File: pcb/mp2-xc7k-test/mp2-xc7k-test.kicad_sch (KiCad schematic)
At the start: 5 parts, among them M5 MECHANICAL, M6 MECHANICAL, M7 MECHANICAL, M8 MECHANICAL, M9 MECHANICAL

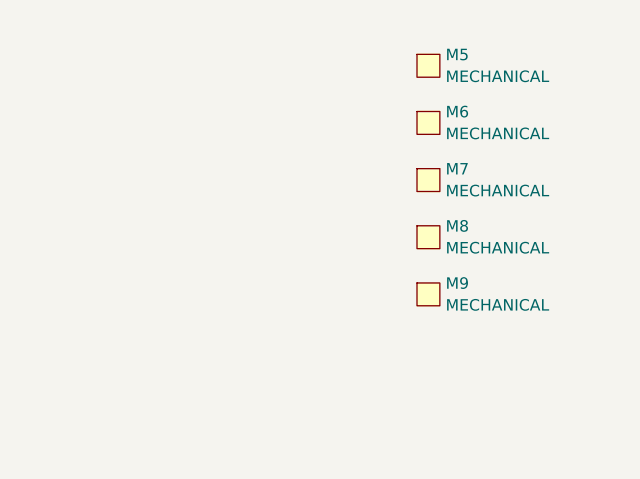
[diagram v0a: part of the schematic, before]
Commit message: Continued layout, 454 unrouted
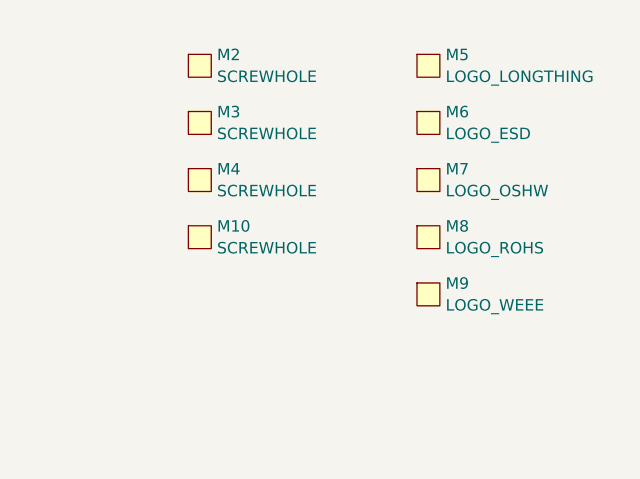
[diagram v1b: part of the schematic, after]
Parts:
- added M10, M2, M3, M4: SCREWHOLE, azonenberg_pcb:MECHANICAL_CLEARANCEHOLE_4_40, symbol special-azonenberg:MECHANICAL
- M5: value MECHANICAL -> LOGO_LONGTHING
- M6: value MECHANICAL -> LOGO_ESD
- M7: value MECHANICAL -> LOGO_OSHW
- M8: value MECHANICAL -> LOGO_ROHS
- M9: value MECHANICAL -> LOGO_WEEE

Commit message: Test board ready for design review
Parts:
- added FID1, FID2, FID3, FID4, FID5, FID6: FIDUCIAL, azonenberg_pcb:FIDUCIAL_1MM, symbol special-azonenberg:MECHANICAL

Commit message: Schematic review complete, added a few more test points
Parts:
- added TP14, TP15: GROUND, azonenberg_pcb:TESTPOINT_SMT_KEYSTONE_5016, symbol conn:CONN_01X01
- added TP16, TP17, TP18: GROUND, azonenberg_pcb:TESTPOINT_BARETRACE_328UM, symbol conn:CONN_01X01
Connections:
- net GND: now also TP14.1 (P1), TP15.1 (P1), TP16.1 (P1), TP17.1 (P1), TP18.1 (P1)

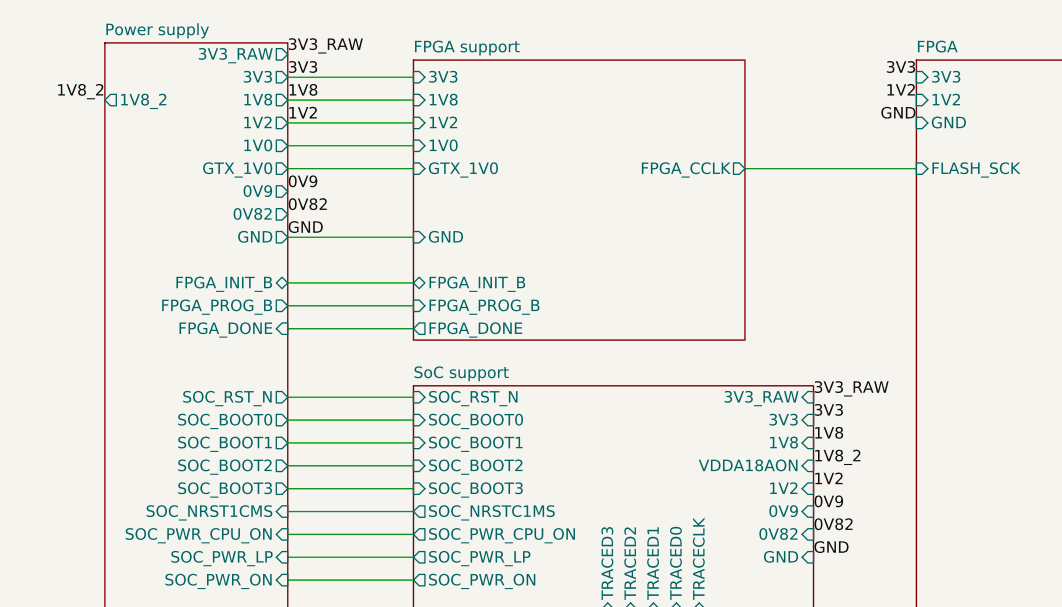
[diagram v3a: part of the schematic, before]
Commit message: Added 1V8_SOC load switch
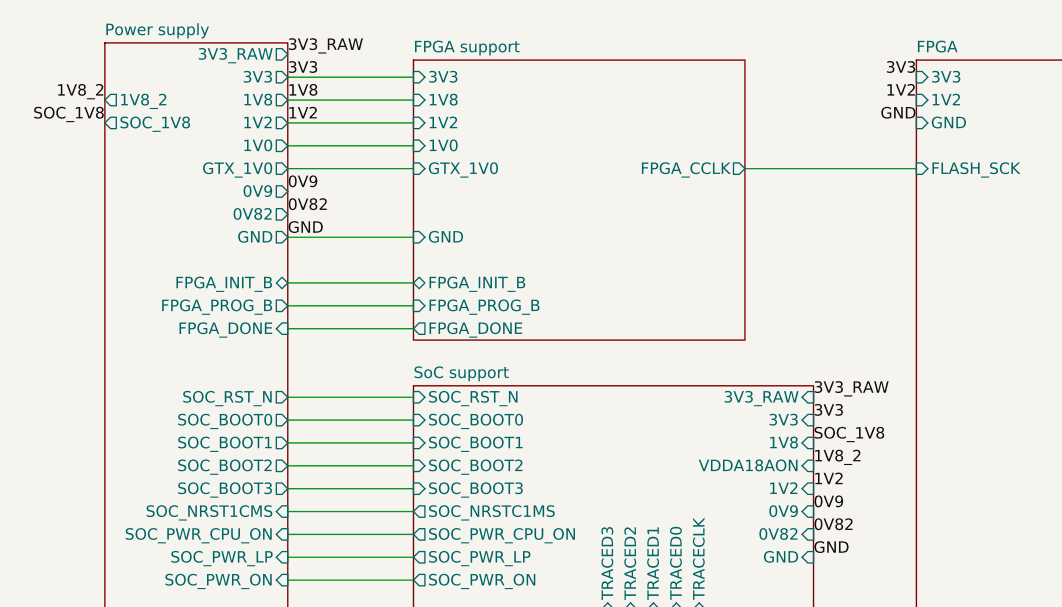
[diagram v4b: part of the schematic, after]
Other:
- sheet Power supply ports: added SOC_1V8; removed none
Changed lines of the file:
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@@
 	(paper "A3")
 	(title_block
-		(date "2025-12-25")
+		(date "2025-12-26")
 		(rev "0.1")
 	)
@@
 		)
 	)
-	(label "1V8"
+	(label "SOC_1V8"
 		(at 104.14 60.96 0)
 		(effects
@@
 	(label "GND"
 		(at 115.57 25.4 180)
+		(effects
+			(font
+				(size 1.27 1.27)
+			)
+			(justify right bottom)
+		)
+	)
+	(label "SOC_1V8"
+		(at 25.4 25.4 180)
 		(effects
 			(font
@@
 			(effects
 				(font
+					(size 1.27 1.27)
+				)
+				(justify left)
+			)
+		)
+		(pin "SOC_1V8" output
+			(at 25.4 25.4 180)
+			(effects
+				(font
